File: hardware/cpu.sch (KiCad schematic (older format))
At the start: 8 parts, among them J8 DEBUG, U3 STM32L011F4P6, U4 ISO7021

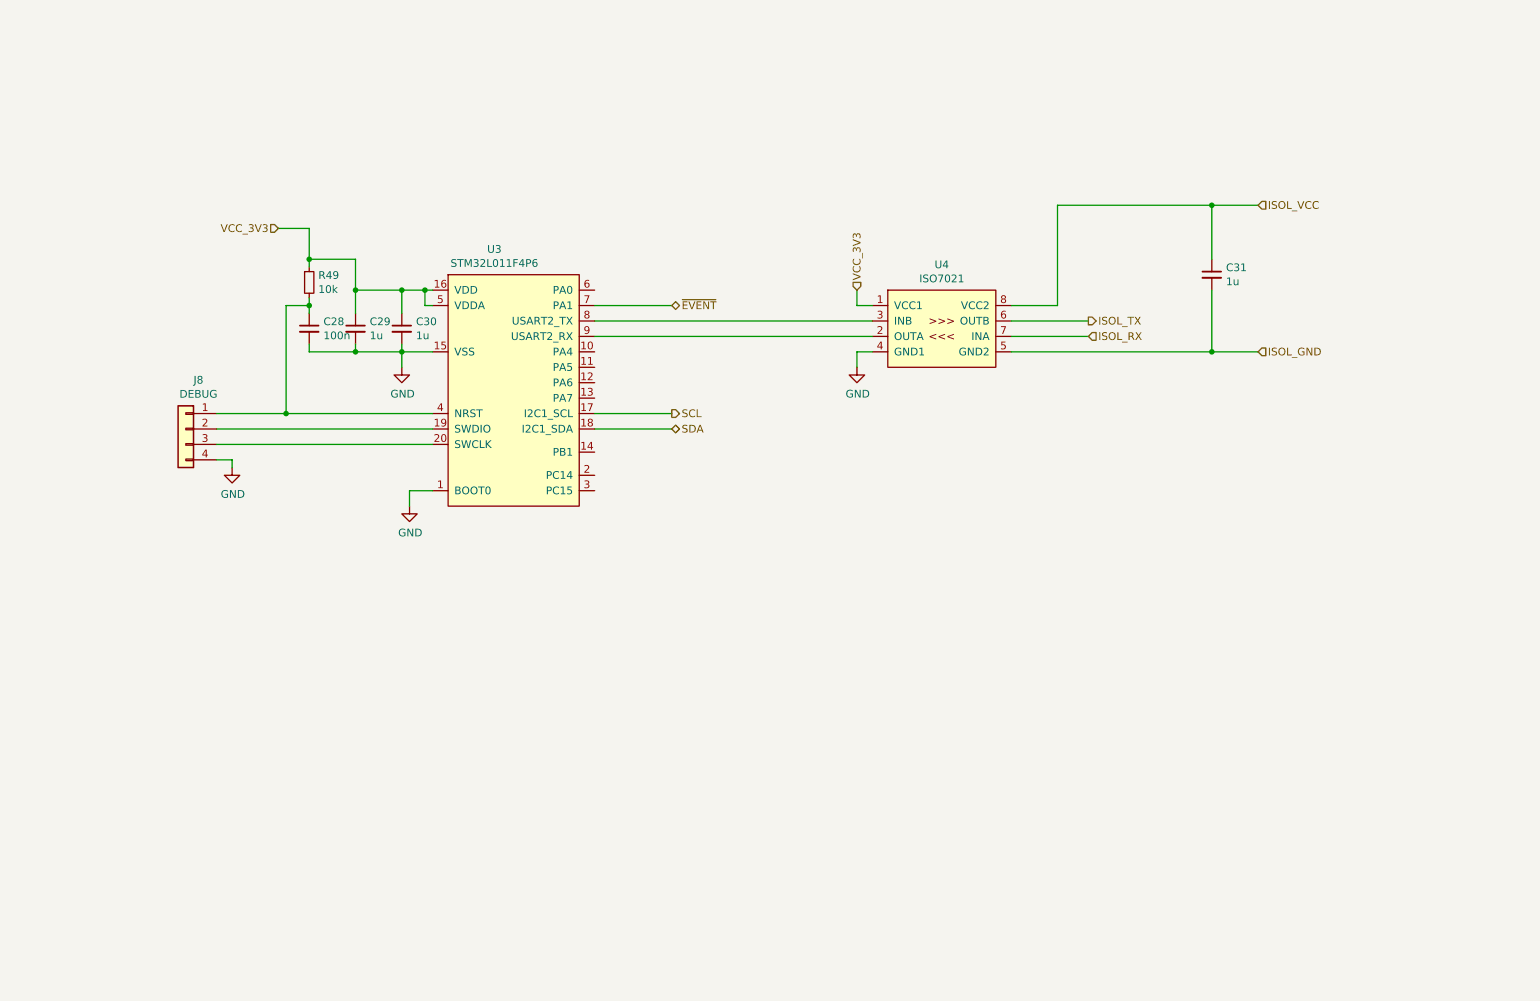
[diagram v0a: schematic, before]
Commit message: finish clean-up and part assignment
Signed-off-by: Ene Alexandru <ene.alexandru@gmail.com>
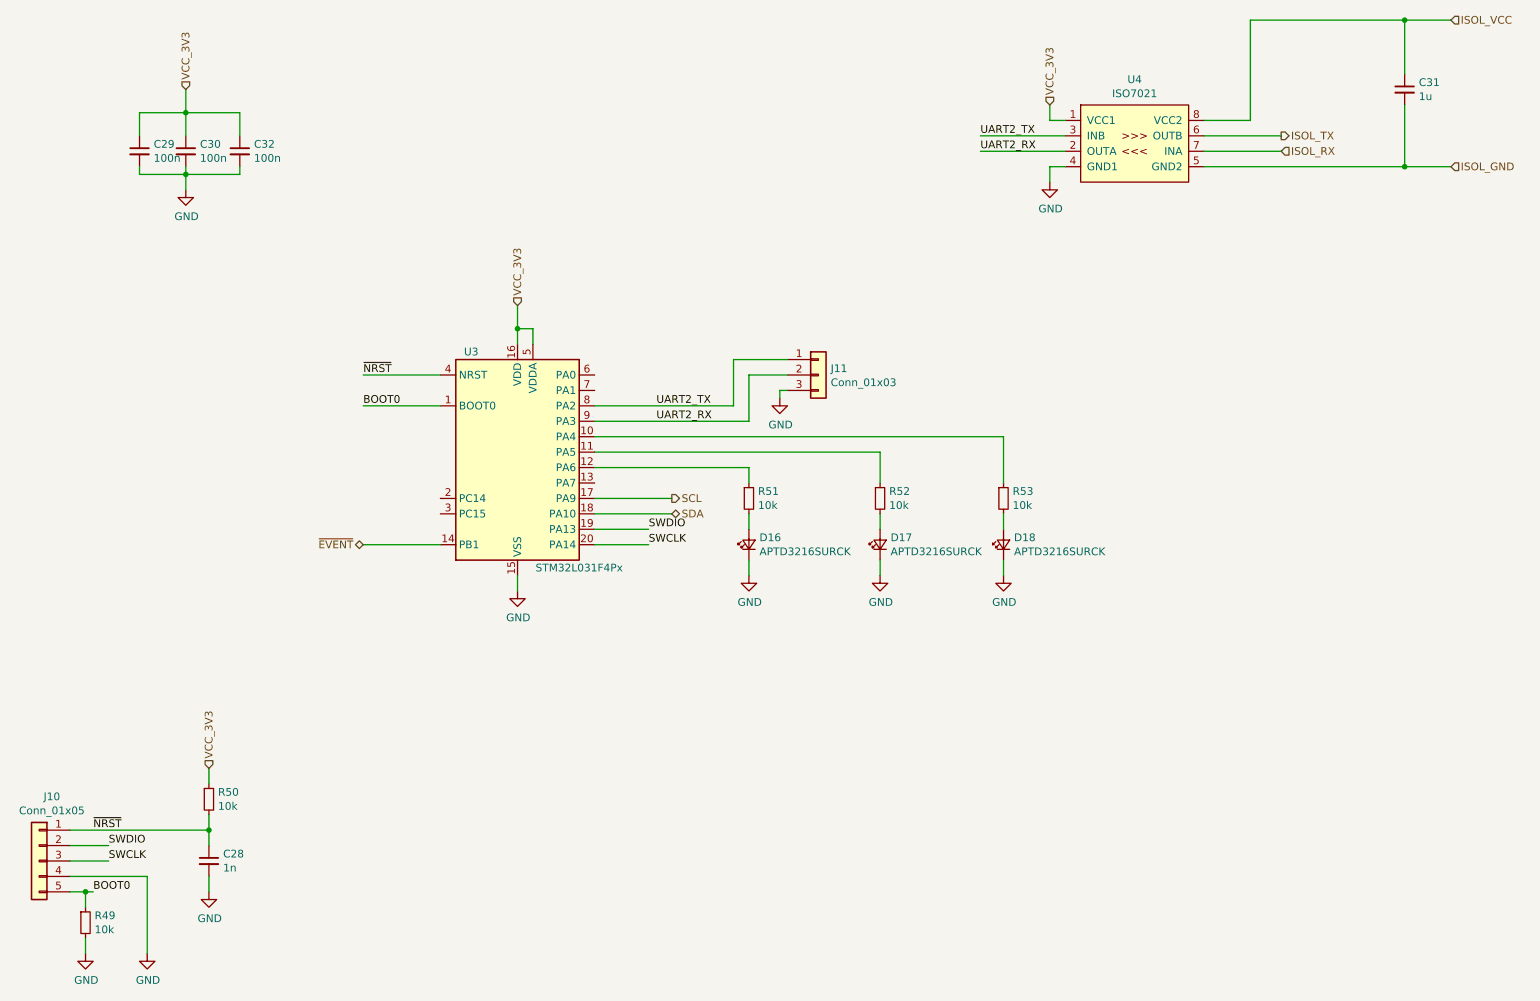
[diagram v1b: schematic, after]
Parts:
- removed J8: DEBUG, Connector_PinHeader_2.54mm:PinHeader_1x04_P2.54mm_Vertical, symbol Connector_Generic:Conn_01x04
- removed U3: STM32L011F4P6, Package_SO:TSSOP-20_4.4x6.5mm_P0.65mm, symbol bms10s:STM32L011F4P6
- added C32: 100n, Capacitor_SMD:C_0805_2012Metric_Pad1.15x1.40mm_HandSolder, symbol Device:C_Small
- added D16, D17, D18: APTD3216SURCK, Capacitor_SMD:C_1206_3216Metric_Pad1.42x1.75mm_HandSolder, symbol Device:LED_Small
- added J10: Conn_01x05, Connector_PinHeader_2.54mm:PinHeader_1x05_P2.54mm_Vertical, symbol Connector_Generic:Conn_01x05
- added J11: Conn_01x03, Connector_PinHeader_2.54mm:PinHeader_1x03_P2.54mm_Vertical, symbol Connector_Generic:Conn_01x03
- added R50, R51, R52, R53: 10k, Resistor_SMD:R_0805_2012Metric_Pad1.15x1.40mm_HandSolder, symbol Device:R_Small
- added U3: STM32L031F4Px, Package_SO:TSSOP-20_4.4x6.5mm_P0.65mm, symbol MCU_ST_STM32L0:STM32L031F4Px
- C28: value 100n -> 1n
- C29, C30: value 1u -> 100n
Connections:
- net GND: now also R49.2, C32.2, D16.1 (K), D17.1 (K), D18.1 (K), J10.4 (Pin_4), J11.3 (Pin_3), U3.15 (VSS)
- net SCL: now also U3.17 (PA9)
- net SDA: now also U3.18 (PA10)
- net VCC_3V3: now also C32.1, R50.1, U3.16 (VDD), U3.5 (VDDA); no longer R49.1
- net ~EVENT: now also U3.14 (PB1)
- net ~NRST: now reaches C28.1
- net ~NRST: now also J10.1 (Pin_1), R50.2, U3.4 (NRST); no longer R49.2
- net UART2_TX: now reaches U4.3 (INB)
- net UART2_TX: now also J11.1 (Pin_1), U3.8 (PA2)
- net UART2_RX: now reaches U4.2 (OUTA)
- net UART2_RX: now also J11.2 (Pin_2), U3.9 (PA3)
- new net: R53.1, U3.10 (PA4)
- new net: R52.1, U3.11 (PA5)
- new net: R51.1, U3.12 (PA6)
- new net: D16.2 (A), R51.2
- new net: D17.2 (A), R52.2
- new net: D18.2 (A), R53.2
- new net BOOT0: J10.5 (Pin_5), R49.1, U3.1 (BOOT0)
- new net SWCLK: J10.3 (Pin_3), U3.20 (PA14)
- new net SWDIO: J10.2 (Pin_2), U3.19 (PA13)
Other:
- moved on the sheet: C28, C29, C30, C31, R49, U4
